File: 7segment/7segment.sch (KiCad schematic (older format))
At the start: 101 parts, among them J1 Conn_01x05_Male, U1 74HC595, U2 74HC595, U3 74HC595, U4 74HC595

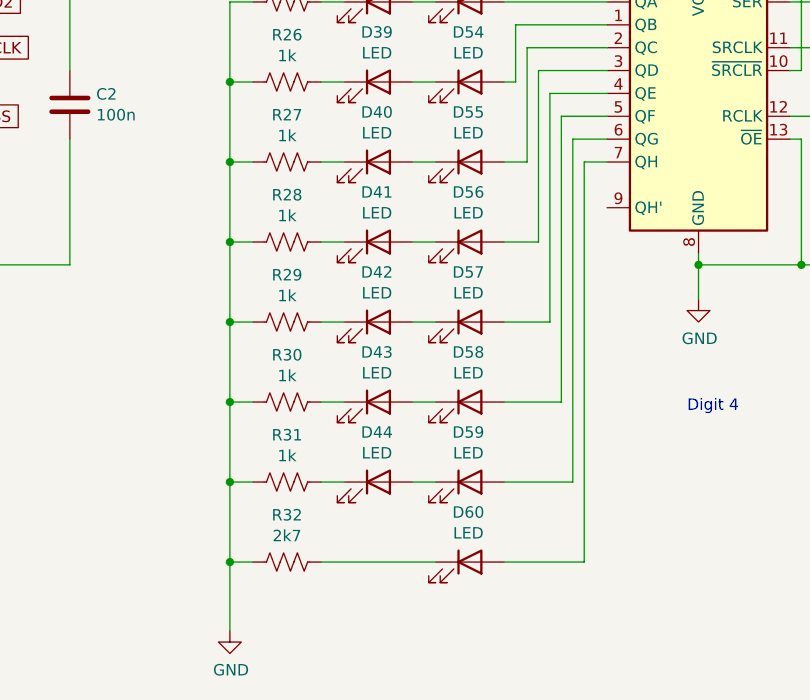
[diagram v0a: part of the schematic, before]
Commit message: resized to <100mm
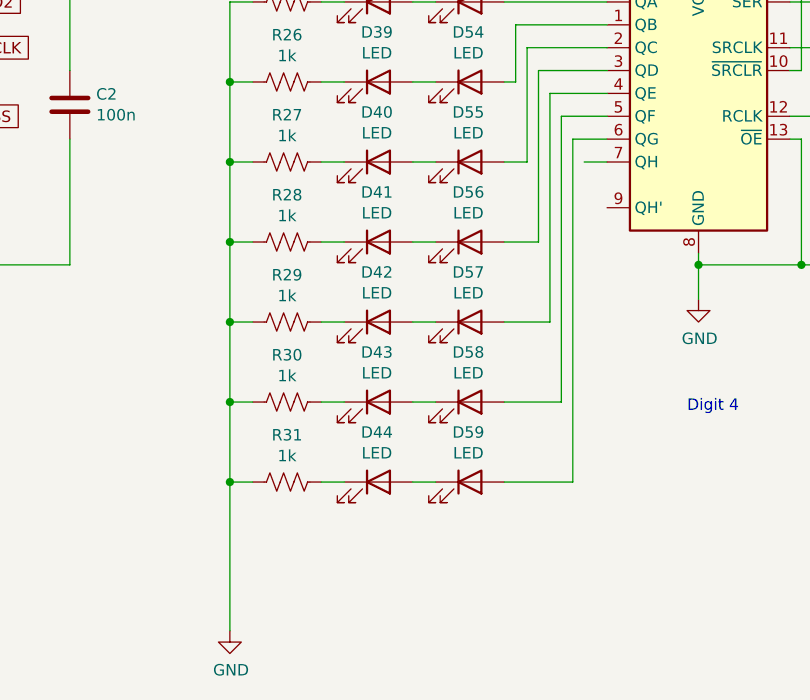
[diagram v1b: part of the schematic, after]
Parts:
- removed D60: LED, LED_THT:LED_D3.0mm, symbol Device:LED
- removed R32: 2k7, Resistor_THT:R_Axial_DIN0204_L3.6mm_D1.6mm_P5.08mm_Horizontal, symbol Device:R_US
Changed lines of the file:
@@
 Wire Wire Line
 	5100 6850 5000 6850
-$Comp
-L Device:R_US R32
-U 1 1 5FE2F55B
-P 4850 7200
-F 0 "R32" V 4645 7200 50  0000 C CNN
-F 1 "2k7" V 4736 7200 50  0000 C CNN
-F 2 "Resistor_THT:R_Axial_DIN0204_L3.6mm_D1.6mm_P5.08mm_Horizontal" V 4890 7190 50  0001 C CNN
-F 3 "~" H 4850 7200 50  0001 C CNN
-	1    4850 7200
-	0    1    1    0
-$EndComp
-$Comp
-L Device:LED D60
-U 1 1 5FE2F561
-P 5650 7200
-F 0 "D60" H 5643 7417 50  0000 C CNN
-F 1 "LED" H 5643 7326 50  0000 C CNN
-F 2 "LED_THT:LED_D3.0mm" H 5650 7200 50  0001 C CNN
-F 3 "~" H 5650 7200 50  0001 C CNN
-	1    5650 7200
-	1    0    0    -1
-$EndComp
 Wire Wire Line
 	5800 5100 5850 5100
@@
 	6100 5350 6250 5350
 Wire Wire Line
-	5800 7200 6150 7200
-Wire Wire Line
-	6150 7200 6150 5450
-Wire Wire Line
 	6150 5450 6250 5450
-Wire Wire Line
-	4700 7200 4600 7200
-Wire Wire Line
-	4600 7200 4600 6850
 Wire Wire Line
 	4600 6850 4700 6850
@@
 Connection ~ 4600 5100
 Wire Wire Line
-	4600 7200 4600 7500
-Connection ~ 4600 7200
-Wire Wire Line
 	6650 5850 6650 5900
 Wire Wire Line
 	6650 4550 6650 4500
-Wire Wire Line
-	5000 7200 5500 7200
 $Comp
 L power:+5V #PWR011
@@
 Wire Wire Line
 	6250 2350 6250 2500
+Wire Wire Line
+	4600 6850 4600 7500
 $EndSCHEMATC

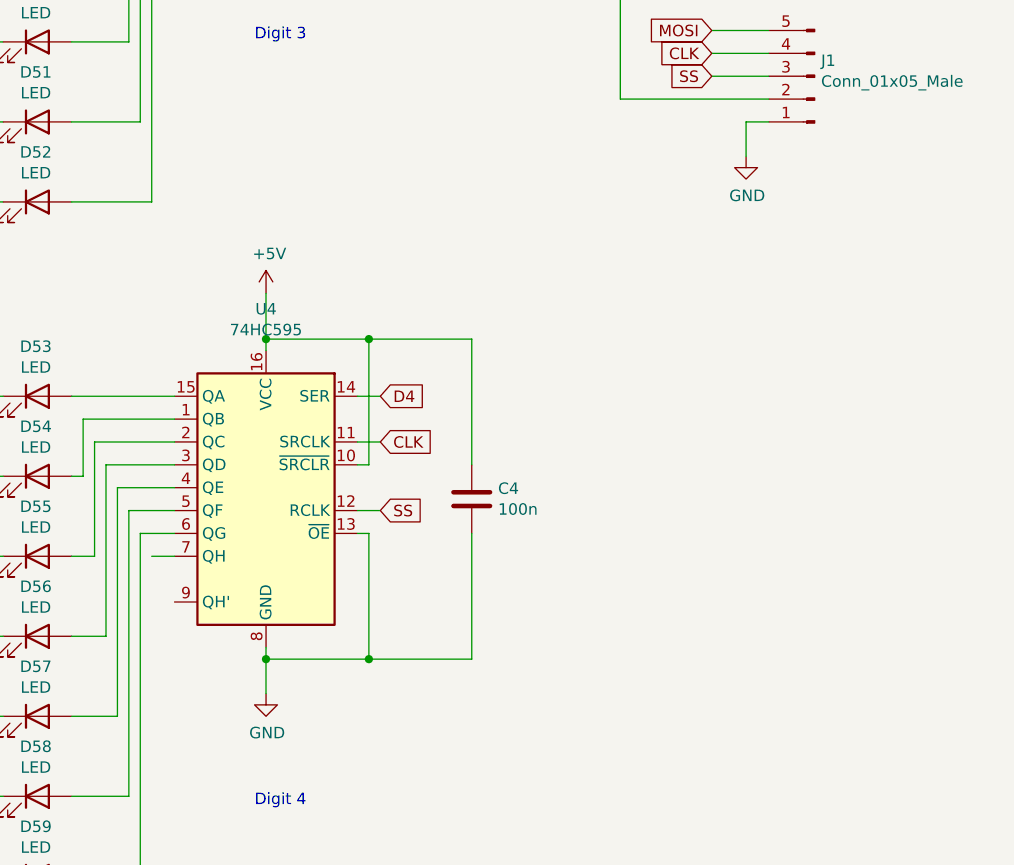
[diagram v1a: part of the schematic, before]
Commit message: Added daisy-chain connector
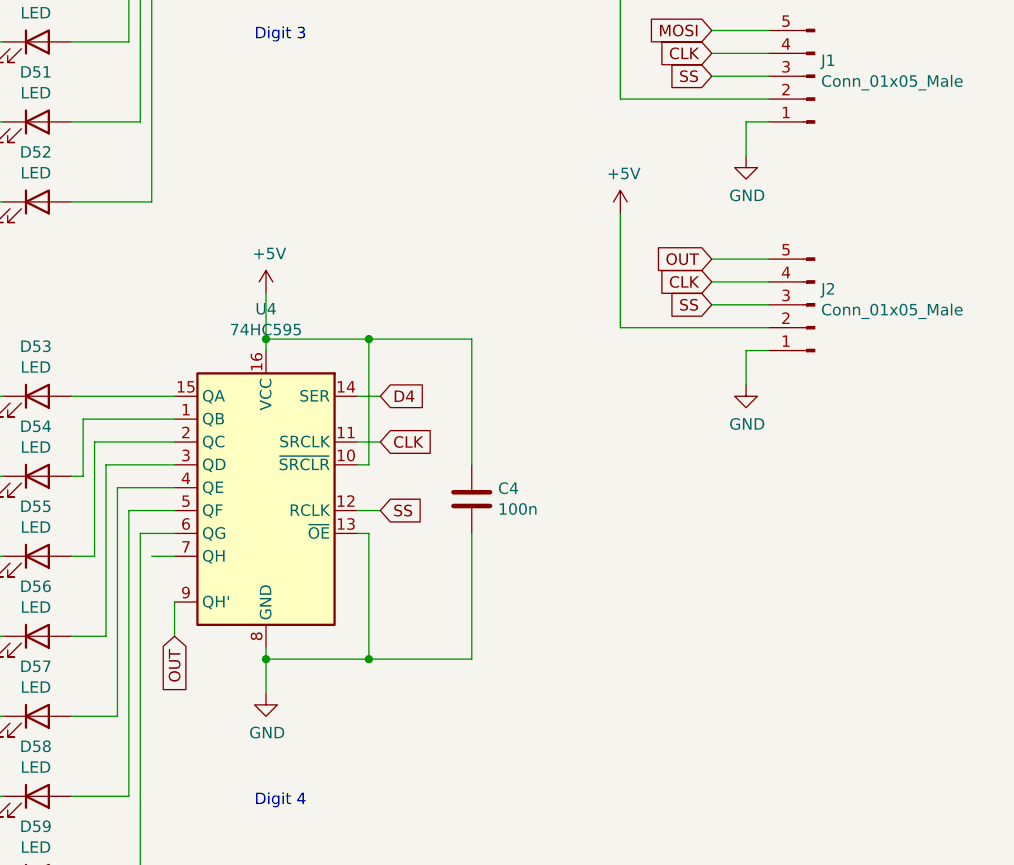
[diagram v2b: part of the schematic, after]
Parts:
- added J2: Conn_01x05_Male, Connector_PinHeader_2.54mm:PinHeader_1x05_P2.54mm_Vertical, symbol Connector:Conn_01x05_Male
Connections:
- net +5V: now also J2.2 (Pin_2)
- net CLK: now also J2.4 (Pin_4)
- net GND: now also J2.1 (Pin_1)
- net SS: now also J2.3 (Pin_3)
- net OUT: now reaches U4.9 (QH')
- net OUT: now also J2.5 (Pin_5)
